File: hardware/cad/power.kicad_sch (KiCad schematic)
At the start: 52 parts, among them J301 JACK, DC, U301 LM337, U302 LM317, U303 ADP5070, U304 LM317

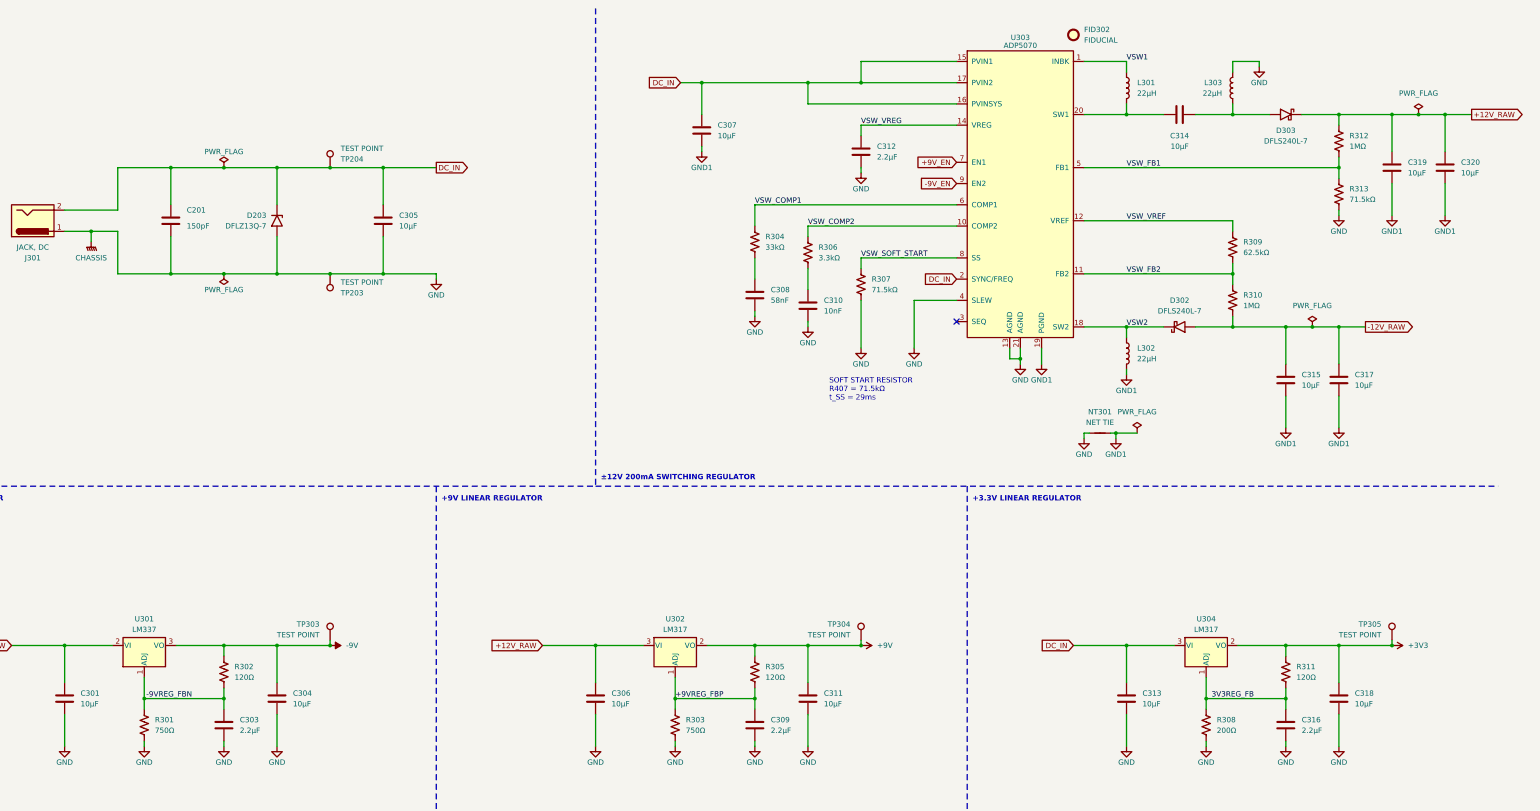
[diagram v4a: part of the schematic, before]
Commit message: board layout first pass
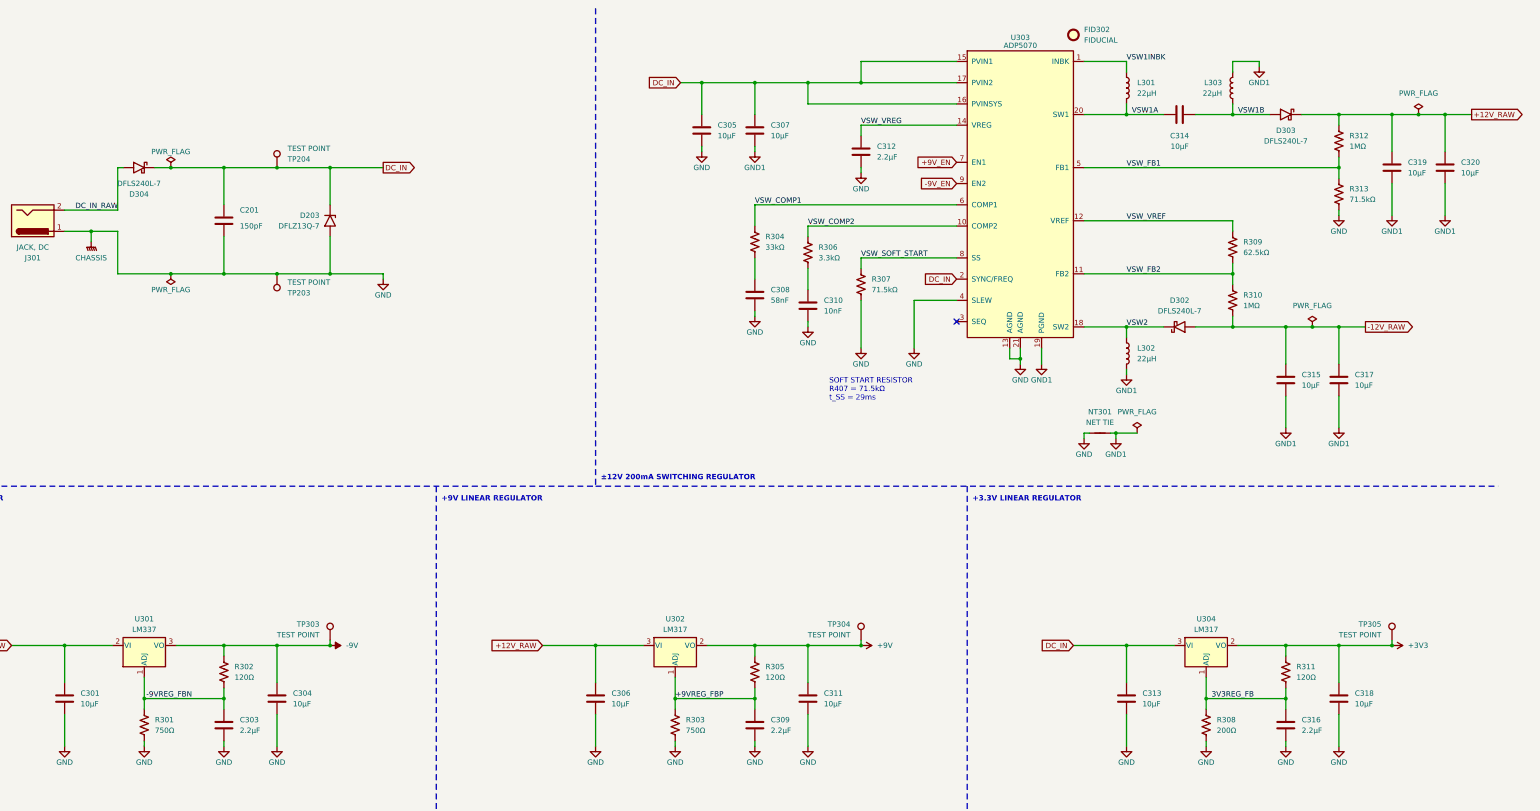
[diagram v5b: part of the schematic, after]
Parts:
- added D304: DFLS240L-7, Library:D_PowerDI-123_THERMAL_PAD, symbol Library:RSX051VAM30TR
- C301, C304, C305, C306, C307, C311, C313, C314, C315, C317, C318, C319, C320: value 10µF -> 10μF
- C303, C309, C312, C316: value 2.2µF -> 2.2μF
- L301, L302, L303: value 22µH -> 22μH; footprint Inductor_SMD:L_Bourns_SRP5030T -> Library:L_TDK_VLS6045EX_VLS6045AF
- R308: footprint Resistor_SMD:R_0603_1608Metric -> Resistor_SMD:R_0402_1005Metric
- TP203, TP204, TP303, TP304, TP305: footprint TestPoint:TestPoint_Plated_Hole_D2.0mm -> TestPoint:TestPoint_Pad_D1.0mm
- U301, U302, U304: footprint Package_TO_SOT_SMD:SOT-223-3_TabPin2 -> Library:TO-252-2_THERMAL_PAD
- U303: footprint Library:LFCSP-20-1EP_4x4mm_P0.5mm_EP2.6x2.6mm -> Library:LFCSP-20-1EP_4x4mm_P0.5mm_EP2.6x2.6mm_ThermalVias
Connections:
- net DC_IN: now also D304.1 (K); no longer J301.2
- net GND: no longer L303.1
- net GND1: now also L303.1
- net VSW1A: now reaches C314.2, L301.2, U303.20 (SW1)
- net VSW1B: now reaches C314.1, D303.2 (A), L303.2
- net VSW1 renamed VSW1INBK
- new net DC_IN_RAW: D304.2 (A), J301.2
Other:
- moved on the sheet: C201, D203, TP203, TP204

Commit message: an inappropriately large commit
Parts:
- C301, C304, C305, C306, C307, C311, C313, C314, C315, C317, C318, C319, C320: Part Number GRM32EC72A106KE05 -> GRM32EC72A106KE05L
- C303, C309, C312, C316: Part Number GRM188R61H225KE11J -> GRM188Z71E225KE43D
- C308: footprint Capacitor_SMD:C_0603_1608Metric -> Capacitor_SMD:C_0805_2012Metric; Manufacturer Murata -> Kemet; Part Number GRM1885C1H202JA01 -> C0805C564K5RAC7800
- C310: Manufacturer Murata -> TDK; Part Number GCD188R71E393KA01 -> CGA3E2X7R1H103K080AA
- J301: value JACK, DC -> PJ-063AH; symbol Connector:Jack-DC -> Library:Barrel_Jack Shielded
- R301, R303: Part Number (none) -> RK73H1ETTP7500F
- R302, R305, R311: Part Number (none) -> RK73H1ETTP1200F
- R304: Part Number (none) -> RK73H1ETTP3302F
- R306: Part Number (none) -> RK73H1ETTP3301F
- R307, R313: Part Number (none) -> RK73H1ETTP7152F
- R308: Part Number (none) -> RK73H1ETTP2000F
- R309: Part Number (none) -> RK73H1ETTP6252F
- R310, R312: Part Number (none) -> RK73H1ETTP1004F
- TP203: value TEST POINT -> GND
- TP204: value TEST POINT -> DC_IN
- TP303: value TEST POINT -> -9V
- TP304: value TEST POINT -> +9V
- TP305: value TEST POINT -> +3V3
- U301: value LM337 -> LM337KVURG3; footprint Library:TO-252-2_THERMAL_PAD -> Library:TO-252-2
- U302, U304: value LM317 -> LM317MDT-TR; footprint Library:TO-252-2_THERMAL_PAD -> Library:TO-252-2; Manufacturer Texas Instruments -> ST Electronics; Part Number LM317EMPX/NOPB -> LM317MDT-TR
- U303: footprint Library:LFCSP-20-1EP_4x4mm_P0.5mm_EP2.6x2.6mm_ThermalVias -> Library:LFCSP-20-1EP_4x4mm_P0.5mm_EP2.6x2.6mm
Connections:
- net GND: now also J301.S1, J301.S2, NT301.2; no longer NT301.1
- net GND1: now also NT301.1; no longer NT301.2
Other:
- company: ALESSANDRO RIZZONI -> Alessandro Rizzoni
- title: BASEBOARD -> Baseboard
